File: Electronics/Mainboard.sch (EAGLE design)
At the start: 10 parts, among them IC1 ER400RTS-02

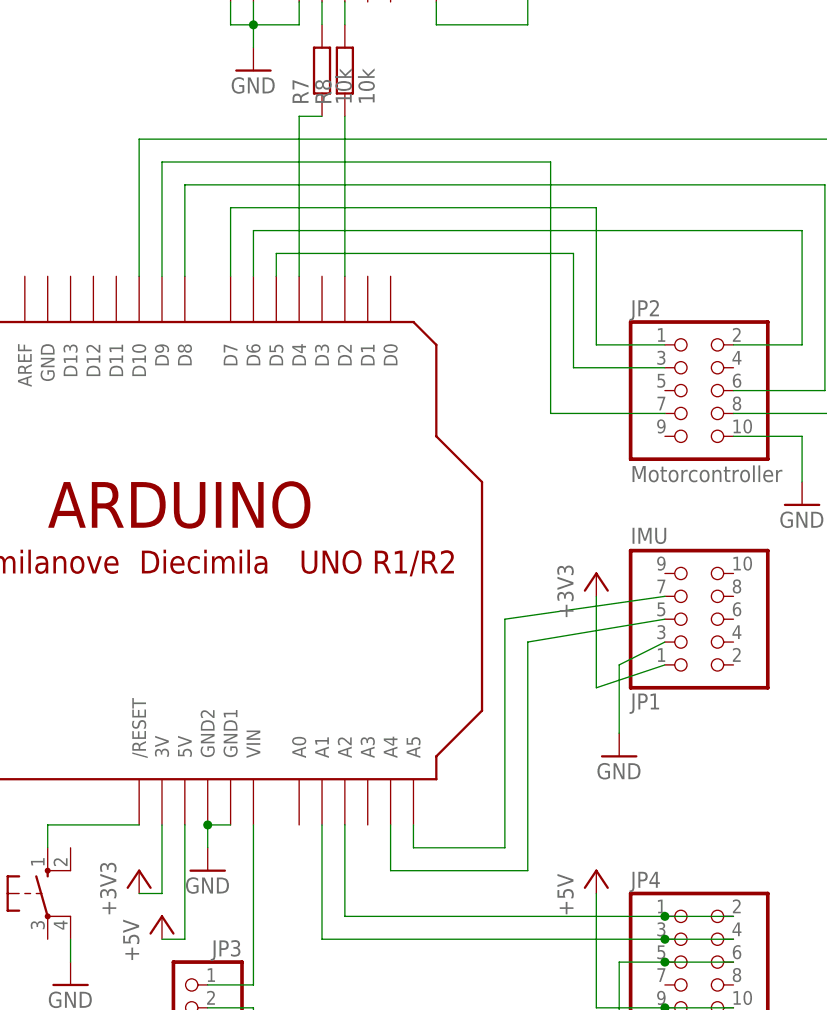
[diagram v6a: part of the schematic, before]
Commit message: Changed pin 5 and 9. Closes #42
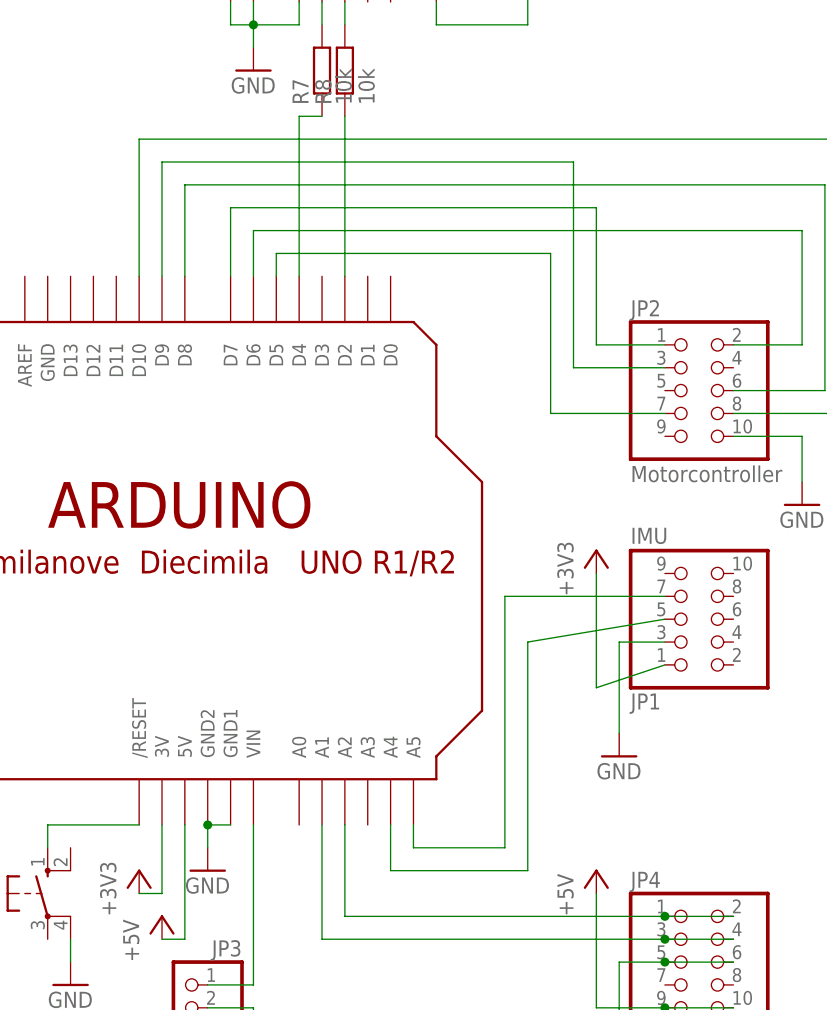
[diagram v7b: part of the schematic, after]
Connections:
- net N$16: now also U$1.D5; no longer U$1.D9
- net N$8: now also U$1.D9; no longer U$1.D5
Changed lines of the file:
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@@
 <instance part="GND6" gate="1" x="66.04" y="76.2"/>
 <instance part="+3V1" gate="G$1" x="-7.62" y="35.56"/>
-<instance part="+3V2" gate="G$1" x="43.18" y="68.58"/>
+<instance part="+3V2" gate="G$1" x="43.18" y="71.12"/>
 <instance part="JP2" gate="A" x="53.34" y="88.9"/>
 <instance part="P+5" gate="1" x="-5.08" y="30.48"/>
@@
 <segment>
 <pinref part="JP1" gate="A" pin="3"/>
-<wire x1="50.8" y1="60.96" x2="45.72" y2="58.42" width="0.1524" layer="91"/>
-<wire x1="45.72" y1="58.42" x2="45.72" y2="50.8" width="0.1524" layer="91"/>
+<wire x1="50.8" y1="60.96" x2="45.72" y2="60.96" width="0.1524" layer="91"/>
+<wire x1="45.72" y1="60.96" x2="45.72" y2="50.8" width="0.1524" layer="91"/>
 <pinref part="GND2" gate="1" pin="GND"/>
 </segment>
@@
 <wire x1="22.86" y1="40.64" x2="22.86" y2="38.1" width="0.1524" layer="91"/>
 <pinref part="JP1" gate="A" pin="7"/>
-<wire x1="50.8" y1="66.04" x2="33.02" y2="63.5" width="0.1524" layer="91"/>
-<wire x1="33.02" y1="63.5" x2="33.02" y2="38.1" width="0.1524" layer="91"/>
+<wire x1="50.8" y1="66.04" x2="33.02" y2="66.04" width="0.1524" layer="91"/>
+<wire x1="33.02" y1="66.04" x2="33.02" y2="38.1" width="0.1524" layer="91"/>
 <wire x1="33.02" y1="38.1" x2="22.86" y2="38.1" width="0.1524" layer="91"/>
 </segment>
@@
 <pinref part="+3V2" gate="G$1" pin="+3V3"/>
 <wire x1="50.8" y1="58.42" x2="43.18" y2="55.88" width="0.1524" layer="91"/>
-<wire x1="43.18" y1="55.88" x2="43.18" y2="66.04" width="0.1524" layer="91"/>
+<wire x1="43.18" y1="55.88" x2="43.18" y2="68.58" width="0.1524" layer="91"/>
 </segment>
 </net>
@@
 <net name="N$8" class="0">
 <segment>
-<wire x1="40.64" y1="91.44" x2="40.64" y2="104.14" width="0.1524" layer="91"/>
-<pinref part="U$1" gate="G$1" pin="D5"/>
-<wire x1="40.64" y1="104.14" x2="7.62" y2="104.14" width="0.1524" layer="91"/>
-<wire x1="7.62" y1="104.14" x2="7.62" y2="101.6" width="0.1524" layer="91"/>
+<wire x1="40.64" y1="91.44" x2="40.64" y2="114.3" width="0.1524" layer="91"/>
+<wire x1="40.64" y1="114.3" x2="-5.08" y2="114.3" width="0.1524" layer="91"/>
 <pinref part="JP2" gate="A" pin="3"/>
 <wire x1="40.64" y1="91.44" x2="50.8" y2="91.44" width="0.1524" layer="91"/>
+<pinref part="U$1" gate="G$1" pin="D9"/>
+<wire x1="-5.08" y1="114.3" x2="-5.08" y2="101.6" width="0.1524" layer="91"/>
 </segment>
 </net>
 <net name="N$16" class="0">
 <segment>
-<pinref part="U$1" gate="G$1" pin="D9"/>
-<wire x1="-5.08" y1="101.6" x2="-5.08" y2="114.3" width="0.1524" layer="91"/>
-<wire x1="-5.08" y1="114.3" x2="38.1" y2="114.3" width="0.1524" layer="91"/>
-<wire x1="38.1" y1="114.3" x2="38.1" y2="86.36" width="0.1524" layer="91"/>
+<wire x1="7.62" y1="104.14" x2="38.1" y2="104.14" width="0.1524" layer="91"/>
+<wire x1="38.1" y1="104.14" x2="38.1" y2="86.36" width="0.1524" layer="91"/>
 <pinref part="JP2" gate="A" pin="7"/>
 <wire x1="38.1" y1="86.36" x2="50.8" y2="86.36" width="0.1524" layer="91"/>
-</segment>
-</net>
+<pinref part="U$1" gate="G$1" pin="D5"/>
+<wire x1="7.62" y1="101.6" x2="7.62" y2="104.14" width="0.1524" layer="91"/>
+</segment>
+</net>
